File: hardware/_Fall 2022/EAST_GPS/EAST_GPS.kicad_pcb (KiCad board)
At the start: 2 copper layers, 30.5 x 25.4 mm, 3 parts, among them J1 Conn_02x08_Odd_Even, U1 GPS-14414, U2 RFM69HCW_Breakout

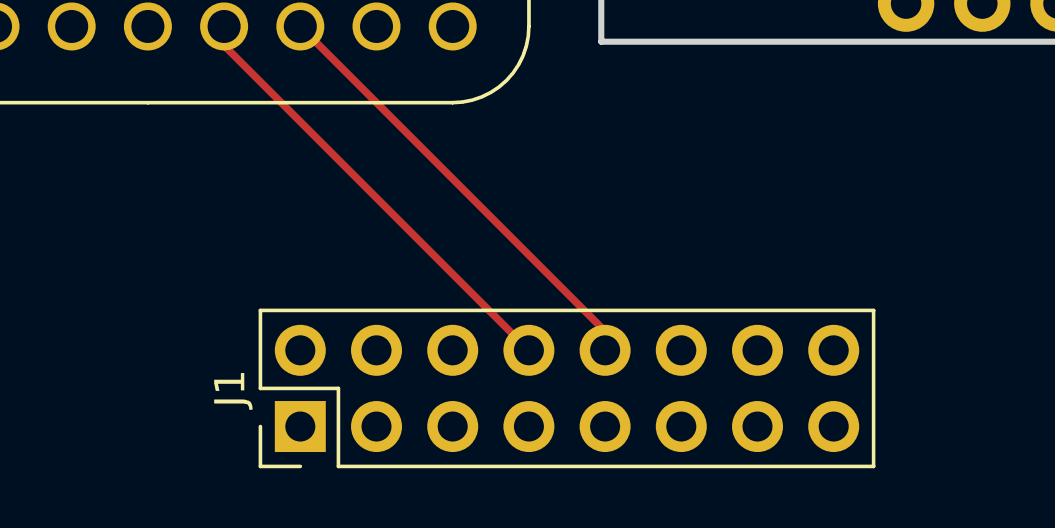
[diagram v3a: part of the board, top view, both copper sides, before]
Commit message: Switch connector pin order on IO
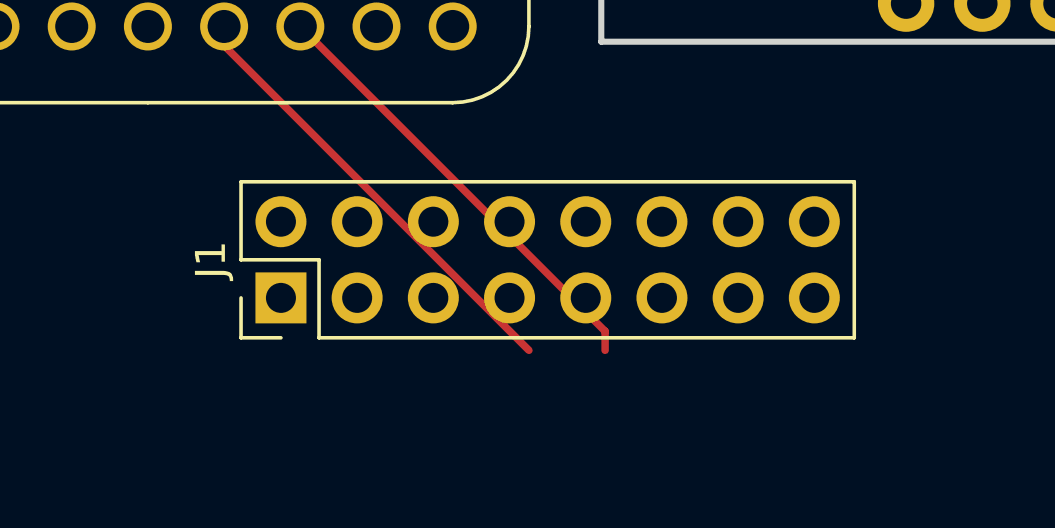
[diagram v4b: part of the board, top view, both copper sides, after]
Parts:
- moved J1 4.34 mm to (131.4, 115.1)
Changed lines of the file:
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@@
   )
   (footprint "Connector_PinHeader_2.54mm:PinHeader_2x08_P2.54mm_Vertical" (layer "F.Cu")
-    (at 132.08 119.38 90)
+    (at 131.4346 115.0924 90)
     (descr "Through hole straight pin header, 2x08, 2.54mm pitch, double rows")
     (tags "Through hole pin header THT 2x08 2.54mm double row")

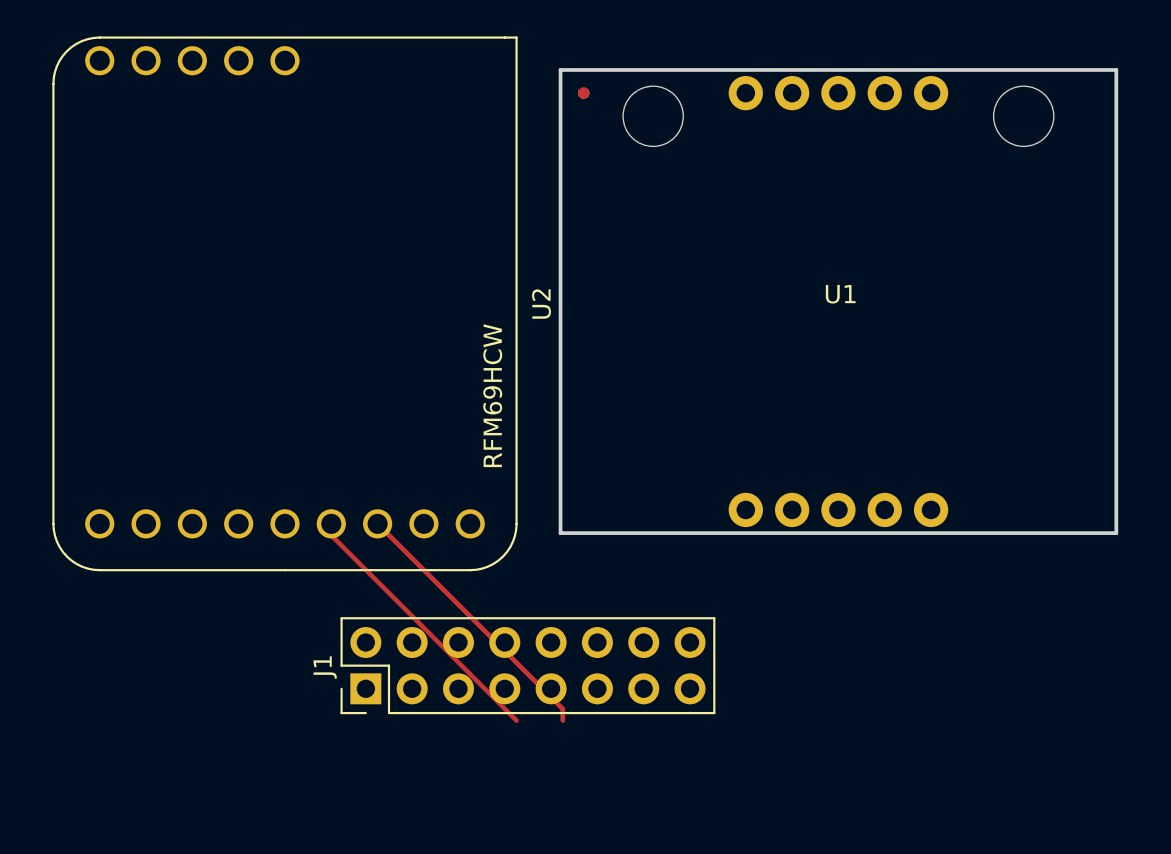
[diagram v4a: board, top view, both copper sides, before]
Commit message: Completed EAST Teensy board, confused at GPS board
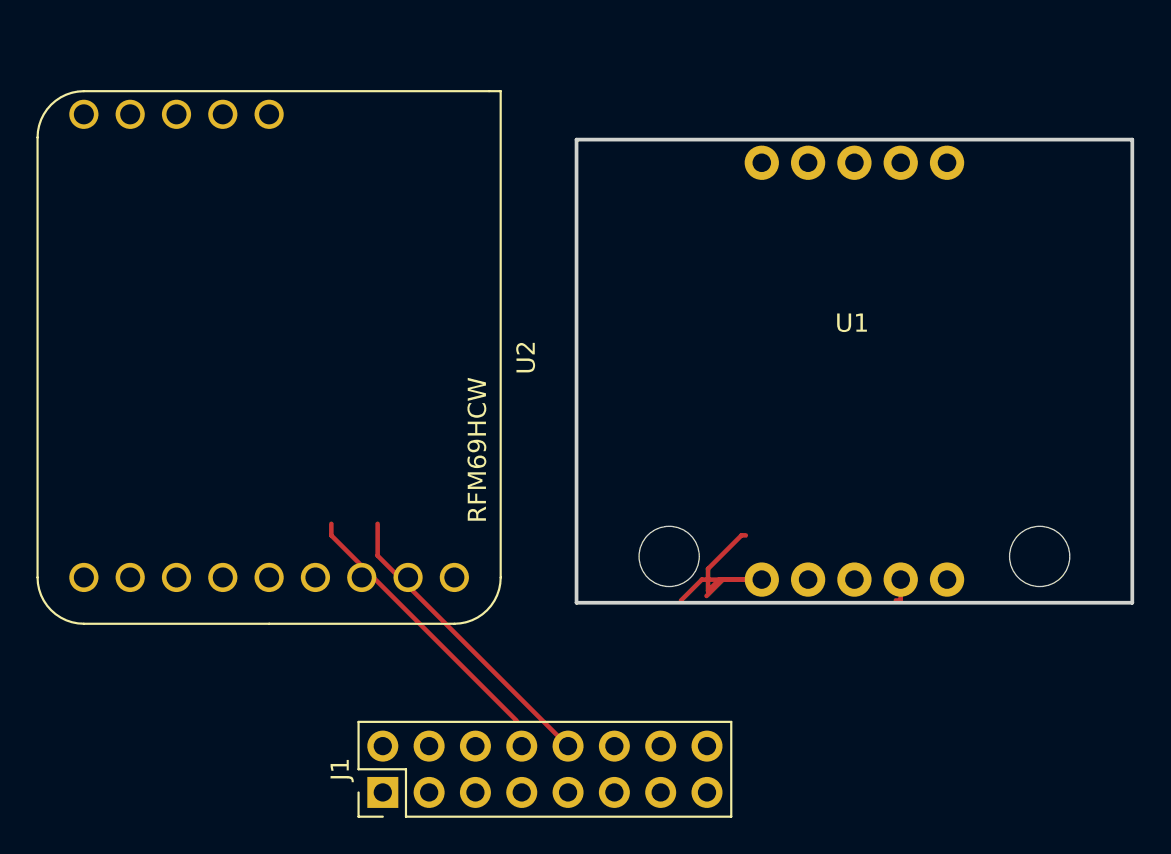
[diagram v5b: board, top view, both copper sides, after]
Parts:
- moved J1 5.76 mm to (132.4, 120.8)
- moved U1 3.62 mm to (158.1, 97.5), turned to 180 degrees
- moved U2 3.07 mm to (126.1, 96.9)
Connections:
- U1 pad 1: (no net) -> unconnected-(U1-Pad1)
- U1 pad 2: (no net) -> /GND
- U1 pad 3: (no net) -> /3.3V
- U1 pad 4: (no net) -> /SDA 2
- U1 pad 5: (no net) -> /SCL 2
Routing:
- net /MISO 1: track 15.0 -> 31.5 mm
- net /SCL 2: track 0.00 -> 15.6 mm
- net /MOSI 1: track 15.0 -> 0.00 mm
- net /GND: track 0.00 -> 1.41 mm
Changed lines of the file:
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@@
   (net 23 "unconnected-(U2-Pad13)")
   (net 24 "unconnected-(U2-Pad14)")
+  (net 25 "unconnected-(U1-Pad1)")
+  (net 26 "unconnected-(U1-Pad6)")
+  (net 27 "unconnected-(U1-Pad7)")
+  (net 28 "unconnected-(U1-Pad8)")
+  (net 29 "unconnected-(U1-Pad9)")
+  (net 30 "unconnected-(U1-Pad10)")
   (footprint "Sensors:RFM69HCW_Breakout" (layer "F.Cu")
-    (at 127 93.98 -90)
-    (property "Sheetfile" "File: EAST_GPS.kicad_sch")
+    (at 126.13 96.92 -90)
+    (property "Sheetfile" "EAST_GPS.kicad_sch")
     (property "Sheetname" "")
     (attr through_hole)
@@
       (effects (font (size 1 1) (thickness 0.15)))
     )
-    (fp_text value "RFM69HCW_Breakout" (at 0 -15.875 90) (layer "F.Fab")
+    (fp_text value "RFM69HCW_Breakout" (at 0 -15.875 90) (layer "F.Fab") hide
       (effects (font (size 1 1) (thickness 0.15)))
     )
@@
   )
   (footprint "GPS_layout:GPS-14414" (layer "F.Cu")
-    (at 157.48 93.98)
-    (property "Sheetfile" "File: EAST_GPS.kicad_sch")
+    (at 158.1027 97.54475 180)
+    (property "Sheetfile" "EAST_GPS.kicad_sch")
     (property "Sheetname" "")
     (attr smd)
-    (fp_text reference "U1" (at 0 -0.5 unlocked) (layer "F.SilkS")
+    (fp_text reference "U1" (at 0 2.5 unlocked) (layer "F.SilkS")
       (effects (font (size 1 1) (thickness 0.15)))
     )
@@
       (effects (font (size 1 1) (thickness 0.15)))
     )
-    (fp_text user "${REFERENCE}" (at 0 2.5 unlocked) (layer "F.Fab")
-      (effects (font (size 1 1) (thickness 0.15)))
-    )
+    (fp_text user "${REFERENCE}" (at 0 -0.5 unlocked) (layer "F.Fab")
+      (effects (font (size 1 1) (thickness 0.15)))
+    )
+    (fp_line (start 15.113 12.573) (end -15.367 12.573) (layer "Edge.Cuts") (width 0.2032))
+    (fp_line (start -15.367 12.573) (end -15.367 -12.827) (layer "Edge.Cuts") (width 0.2032))
     (fp_line (start -15.367 -12.827) (end 15.113 -12.827) (layer "Edge.Cuts") (width 0.2032))
-    (fp_line (start -15.367 12.573) (end -15.367 -12.827) (layer "Edge.Cuts") (width 0.2032))
     (fp_line (start 15.113 -12.827) (end 15.113 12.573) (layer "Edge.Cuts") (width 0.2032))
-    (fp_line (start 15.113 12.573) (end -15.367 12.573) (layer "Edge.Cuts") (width 0.2032))
     (fp_circle (center -10.287 -10.287) (end -7.493 -10.287) (layer "F.CrtYd") (width 0.127) (fill none))
     (fp_circle (center 10.033 -10.287) (end 12.827 -10.287) (layer "F.CrtYd") (width 0.127) (fill none))
-    (pad "" np_thru_hole circle (at 10.033 -10.287) (size 3.302 3.302) (drill 3.302) (layers *.Cu *.Mask))
-    (pad "" np_thru_hole circle (at -10.287 -10.287) (size 3.302 3.302) (drill 3.302) (layers *.Cu *.Mask))
-    (pad "1" thru_hole circle (at -5.207 11.303 90) (size 1.8796 1.8796) (drill 1.016) (layers *.Cu *.Mask)
-      (solder_mask_margin 0.1016))
-    (pad "1" smd roundrect (at -14.097 -11.557 180) (size 0.635 0.635) (layers "B.Cu" "B.Mask") (roundrect_rratio 0.5)
-      (solder_mask_margin 0.1016))
-    (pad "1" thru_hole circle (at -5.207 -11.557 90) (size 1.8796 1.8796) (drill 1.016) (layers *.Cu *.Mask)
-      (solder_mask_margin 0.1016))
-    (pad "1" thru_hole circle (at -2.667 11.303 90) (size 1.8796 1.8796) (drill 1.016) (layers *.Cu *.Mask)
-      (solder_mask_margin 0.1016))
-    (pad "1" smd roundrect (at -14.097 -11.557) (size 0.635 0.635) (layers "F.Cu" "F.Mask") (roundrect_rratio 0.5)
-      (solder_mask_margin 0.1016))
-    (pad "2" thru_hole circle (at -0.127 11.303 90) (size 1.8796 1.8796) (drill 1.016) (layers *.Cu *.Mask)
-      (solder_mask_margin 0.1016))
-    (pad "2" thru_hole circle (at -2.667 -11.557 90) (size 1.8796 1.8796) (drill 1.016) (layers *.Cu *.Mask)
-      (solder_mask_margin 0.1016))
-    (pad "3" thru_hole circle (at -0.127 -11.557 90) (size 1.8796 1.8796) (drill 1.016) (layers *.Cu *.Mask)
-      (solder_mask_margin 0.1016))
-    (pad "3" thru_hole circle (at 2.413 11.303 90) (size 1.8796 1.8796) (drill 1.016) (layers *.Cu *.Mask)
-      (solder_mask_margin 0.1016))
-    (pad "4" thru_hole circle (at 4.953 11.303 90) (size 1.8796 1.8796) (drill 1.016) (layers *.Cu *.Mask)
-      (solder_mask_margin 0.1016))
-    (pad "4" thru_hole circle (at 2.413 -11.557 90) (size 1.8796 1.8796) (drill 1.016) (layers *.Cu *.Mask)
-      (solder_mask_margin 0.1016))
-    (pad "5" thru_hole circle (at 4.953 -11.557 90) (size 1.8796 1.8796) (drill 1.016) (layers *.Cu *.Mask)
-      (solder_mask_margin 0.1016))
+    (fp_poly (pts
+        (xy 14.986 12.954)
+        (xy 15.494 12.954)
+        (xy 15.494 12.446)
+        (xy 14.986 12.446)
+      ) (layer "F.Fab") (width 0) (fill solid))
+    (pad "" np_thru_hole circle (at -10.287 -10.287 180) (size 3.302 3.302) (drill 3.302) (layers *.Cu *.Mask))
+    (pad "" np_thru_hole circle (at 10.033 -10.287 180) (size 3.302 3.302) (drill 3.302) (layers *.Cu *.Mask))
+    (pad "1" thru_hole circle (at -5.207 -11.557 270) (size 1.8796 1.8796) (drill 1.016) (layers *.Cu *.Mask)
+      (net 25 "unconnected-(U1-Pad1)") (pinfunction "INT") (pintype "output+no_connect") (solder_mask_margin 0.1016))
+    (pad "2" thru_hole circle (at -2.667 -11.557 270) (size 1.8796 1.8796) (drill 1.016) (layers *.Cu *.Mask)
+      (net 1 "/GND") (pinfunction "GND") (pintype "power_in") (solder_mask_margin 0.1016))
+    (pad "3" thru_hole circle (at -0.127 -11.557 270) (size 1.8796 1.8796) (drill 1.016) (layers *.Cu *.Mask)
+      (net 2 "/3.3V") (pinfunction "3.3V") (pintype "power_in") (solder_mask_margin 0.1016))
+    (pad "4" thru_hole circle (at 2.413 -11.557 270) (size 1.8796 1.8796) (drill 1.016) (layers *.Cu *.Mask)
+      (net 13 "/SDA 2") (pinfunction "SDA") (pintype "output") (solder_mask_margin 0.1016))
+    (pad "5" thru_hole circle (at 4.953 -11.557 270) (size 1.8796 1.8796) (drill 1.016) (layers *.Cu *.Mask)
+      (net 14 "/SCL 2") (pinfunction "SCL") (pintype "output") (solder_mask_margin 0.1016))
+    (pad "6" thru_hole circle (at -5.207 11.303 270) (size 1.8796 1.8796) (drill 1.016) (layers *.Cu *.Mask)
+      (net 26 "unconnected-(U1-Pad6)") (pinfunction "WAKE") (pintype "input+no_connect") (solder_mask_margin 0.1016))
+    (pad "7" thru_hole circle (at -2.667 11.303 270) (size 1.8796 1.8796) (drill 1.016) (layers *.Cu *.Mask)
+      (net 27 "unconnected-(U1-Pad7)") (pinfunction "RST") (pintype "input+no_connect") (solder_mask_margin 0.1016))
+    (pad "8" thru_hole circle (at -0.127 11.303 270) (size 1.8796 1.8796) (drill 1.016) (layers *.Cu *.Mask)
+      (net 28 "unconnected-(U1-Pad8)") (pinfunction "PPS") (pintype "output+no_connect") (solder_mask_margin 0.1016))
+    (pad "9" thru_hole circle (at 2.413 11.303 270) (size 1.8796 1.8796) (drill 1.016) (layers *.Cu *.Mask)
+      (net 29 "unconnected-(U1-Pad9)") (pinfunction "RX") (pintype "input+no_connect") (solder_mask_margin 0.1016))
+    (pad "10" thru_hole circle (at 4.953 11.303 270) (size 1.8796 1.8796) (drill 1.016) (layers *.Cu *.Mask)
+      (net 30 "unconnected-(U1-Pad10)") (pinfunction "TX") (pintype "output+no_connect") (solder_mask_margin 0.1016))
   )
   (footprint "Connector_PinHeader_2.54mm:PinHeader_2x08_P2.54mm_Vertical" (layer "F.Cu")
-    (at 131.4346 115.0924 90)
+    (at 132.365 120.775 90)
     (descr "Through hole straight pin header, 2x08, 2.54mm pitch, double rows")
     (tags "Through hole pin header THT 2x08 2.54mm double row")
-    (property "Sheetfile" "File: EAST_GPS.kicad_sch")
+    (property "Sheetfile" "EAST_GPS.kicad_sch")
     (property "Sheetname" "")
     (attr through_hole)
@@
       (effects (font (size 1 1) (thickness 0.15)))
     )
-    (fp_text value "Conn_02x08_Odd_Even" (at 1.27 20.11 90) (layer "F.Fab")
+    (fp_text value "Conn_02x08_Odd_Even" (at 1.27 20.11 90) (layer "F.Fab") hide
       (effects (font (size 1 1) (thickness 0.15)))
     )
@@
   (gr_line (start 128.8288 116.8654) (end 154.2288 116.8654) (layer "Dwgs.User") (width 0.2))
   (gr_line (start 116.328019 128.2954) (end 166.729581 128.2954) (layer "Dwgs.User") (width 0.2))
-  (segment (start 139.7 116.84) (end 129.54 106.68) (width 0.25) (layer "F.Cu") (net 3))
-  (segment (start 129.54 106.68) (end 129.54 106.045) (width 0.25) (layer "F.Cu") (net 3))
-  (segment (start 142.24 116.205) (end 142.24 116.84) (width 0.25) (layer "F.Cu") (net 4))
-  (segment (start 132.08 106.045) (end 142.24 116.205) (width 0.25) (layer "F.Cu") (net 4))
+  (segment (start 160.7697 110.24675) (end 160.5 110.24675) (width 0.25) (layer "F.Cu") (net 1))
+  (segment (start 160.7697 109.10175) (end 160.7697 110.24675) (width 0.25) (layer "F.Cu") (net 1))
+  (segment (start 132.08 107.79) (end 142.525 118.235) (width 0.25) (layer "F.Cu") (net 4))
+  (segment (start 139.7 116.84) (end 129.54 106.68) (width 0.25) (layer "F.Cu") (net 4))
+  (segment (start 132.08 106.045) (end 132.08 107.79) (width 0.25) (layer "F.Cu") (net 4))
+  (segment (start 129.54 106.68) (end 129.54 106.045) (width 0.25) (layer "F.Cu") (net 4))
+  (segment (start 150.81825 109.10175) (end 150.2 109.72) (width 0.25) (layer "F.Cu") (net 14))
+  (segment (start 149.865 109.10175) (end 148.72 110.24675) (width 0.25) (layer "F.Cu") (net 14))
+  (segment (start 150.2 108.51) (end 152.032 106.678) (width 0.25) (layer "F.Cu") (net 14))
+  (segment (start 150.2 109.72) (end 150.2 108.51) (width 0.25) (layer "F.Cu") (net 14))
+  (segment (start 152.032 106.678) (end 152.273 106.678) (width 0.25) (layer "F.Cu") (net 14))
+  (segment (start 151.01825 109.10175) (end 153.1497 109.10175) (width 0.25) (layer "F.Cu") (net 14))
+  (segment (start 153.1497 109.10175) (end 150.81825 109.10175) (width 0.25) (layer "F.Cu") (net 14))
+  (segment (start 153.1497 109.10175) (end 149.865 109.10175) (width 0.25) (layer "F.Cu") (net 14))
+  (segment (start 151.01825 109.10175) (end 150.12 110) (width 0.25) (layer "F.Cu") (net 14))
   (group "" (id 16c30f42-175b-400f-b540-6040af78e635)
     (members
